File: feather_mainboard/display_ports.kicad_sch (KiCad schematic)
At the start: 1 part, among them J1 61300811121

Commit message: finished daughter board
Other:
- note added: "Need to change the connector"
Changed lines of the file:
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@@
+		)
+	)
+	(text "Need to change the connector"
+		(exclude_from_sim no)
+		(at 138.684 70.612 0)
+		(effects
+			(font
+				(size 10 10)
+				(thickness 4)
+				(bold yes)
+			)
 		)
 	)

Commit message: finished mainboard design, need to do the routing
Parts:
- removed J1: 61300811121, Custom footprints:61300811121, symbol 6130XX11121_61300811121:6130XX11121_61300811121
- added J1: 61900819521, Custom footprints:61900819521, symbol 61900819521:61900819521
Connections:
- net BUSY: now also J1.1
- net CS: now also J1.4
- net DC: now also J1.3
- net DIN: now also J1.6
- net GND: now also J1.7
- net RST: now also J1.2
- net SCLK: now also J1.5
- net VCC: now also J1.8
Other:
- note removed: "Need to change the connector"
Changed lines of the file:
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@@
-		)
-	)
-	(text "Need to change the connector"
-		(exclude_from_sim no)
-		(at 138.684 70.612 0)
-		(effects
-			(font
-				(size 10 10)
-				(thickness 4)
-				(bold yes)
-			)
 		)
 	)
@@
 	)
 	(symbol
-		(lib_id "6130XX11121_61300811121:6130XX11121_61300811121")
+		(lib_id "61900819521:61900819521")
 		(at 153.67 90.17 270)
 		(unit 1)
@@
 		(dnp no)
 		(property "Reference" "J1"
-			(at 151.13 80.264 90)
+			(at 151.384 80.01 90)
 			(effects
 				(font
@@
 			)
 		)
-		(property "Value" "61300811121"
-			(at 146.812 79.248 90)
-			(effects
-				(font
-					(size 1.27 1.27)
-				)
-				(justify left)
-				(hide yes)
-			)
-		)
-		(property "Footprint" "Custom footprints:61300811121"
+		(property "Value" "61900819521"
+			(at 153.67 90.17 0)
+			(effects
+				(font
+					(size 1.27 1.27)
+				)
+				(justify bottom)
+				(hide yes)
+			)
+		)
+		(property "Footprint" "Custom footprints:61900819521"
 			(at 153.67 90.17 0)
 			(effects
@@
 			)
 		)
-		(property "ROWS" "Single"
-			(at 153.67 90.17 0)
-			(effects
-				(font
-					(size 1.27 1.27)
-				)
-				(justify bottom)
-				(hide yes)
-			)
-		)
-		(property "GENDER" "Pin Header"
+		(property "MF" "Würth Elektronik"
+			(at 153.67 90.17 0)
+			(effects
+				(font
+					(size 1.27 1.27)
+				)
+				(justify bottom)
+				(hide yes)
+			)
+		)
+		(property "CONTACT-RESISTANCE" "20mOhm"
+			(at 153.67 90.17 0)
+			(effects
+				(font
+					(size 1.27 1.27)
+				)
+				(justify bottom)
+				(hide yes)
+			)
+		)
+		(property "Description_1" "\n                        \n                            EMI Gaskets, Sheets, Absorbers & Shielding\n                        \n"
+			(at 153.67 90.17 0)
+			(effects
+				(font
+					(size 1.27 1.27)
+				)
+				(justify bottom)
+				(hide yes)
+			)
+		)
+		(property "Package" "None"
+			(at 153.67 90.17 0)
+			(effects
+				(font
+					(size 1.27 1.27)
+				)
+				(justify bottom)
+				(hide yes)
+			)
+		)
+		(property "GENDER" "Male"
 			(at 153.67 90.17 0)
 			(effects
@@
 			)
 		)
-		(property "IR" "3A"
-			(at 153.67 90.17 0)
-			(effects
-				(font
-					(size 1.27 1.27)
-				)
-				(justify bottom)
-				(hide yes)
-			)
-		)
-		(property "VALUE" "61300811121"
+		(property "PITCH" "2.54mm"
+			(at 153.67 90.17 0)
+			(effects
+				(font
+					(size 1.27 1.27)
+				)
+				(justify bottom)
+				(hide yes)
+			)
+		)
+		(property "Check_prices" "https://www.snapeda.com/parts/61900819521/Wurth+Elektronik/view-part/?ref=eda"
+			(at 153.67 90.17 0)
+			(effects
+				(font
+					(size 1.27 1.27)
+				)
+				(justify bottom)
+				(hide yes)
+			)
+		)
+		(property "L" "20.32mm"
+			(at 153.67 90.17 0)
+			(effects
+				(font
+					(size 1.27 1.27)
+				)
+				(justify bottom)
+				(hide yes)
+			)
+		)
+		(property "Price" "None"
 			(at 153.67 90.17 0)
 			(effects
@@
 			)
 		)
+		(property "PART-NUMBER" "61900819521"
+			(at 153.67 90.17 0)
+			(effects
+				(font
+					(size 1.27 1.27)
+				)
+				(justify bottom)
+				(hide yes)
+			)
+		)
+		(property "SnapEDA_Link" "https://www.snapeda.com/parts/61900819521/Wurth+Elektronik/view-part/?ref=snap"
+			(at 153.67 90.17 0)
+			(effects
+				(font
+					(size 1.27 1.27)
+				)
+				(justify bottom)
+				(hide yes)
+			)
+		)
+		(property "DATASHEET-URL" "https://www.we-online.com/redexpert/spec/61900819521?ae"
+			(at 153.67 90.17 0)
+			(effects
+				(font
+					(size 1.27 1.27)
+				)
+				(justify bottom)
+				(hide yes)
+			)
+		)
+		(property "MP" "61900819521"
+			(at 153.67 90.17 0)
+			(effects
+				(font
+					(size 1.27 1.27)
+				)
+				(justify bottom)
+				(hide yes)
+			)
+		)
+		(property "WORKING-VOLTAGE" "250V(AC)"
+			(at 153.67 90.17 0)
+			(effects
+				(font
+					(size 1.27 1.27)
+				)
+				(justify bottom)
+				(hide yes)
+			)
+		)
 		(property "PINS" "8"
 			(at 153.67 90.17 0)
@@
 			)
 		)
-		(property "DATASHEET-URL" "https://www.we-online.com/redexpert/spec/61300811121?ae"
-			(at 153.67 90.17 0)
-			(effects
-				(font
-					(size 1.27 1.27)
-				)
-				(justify bottom)
-				(hide yes)
-			)
-		)
-		(property "PITCH" "2.54mm"
-			(at 153.67 90.17 0)
-			(effects
-				(font
-					(size 1.27 1.27)
-				)
-				(justify bottom)
-				(hide yes)
-			)
-		)
-		(property "PART-NUMBER" "61300811121"
-			(at 153.67 90.17 0)
-			(effects
-				(font
-					(size 1.27 1.27)
-				)
-				(justify bottom)
-				(hide yes)
-			)
-		)
-		(property "TYPE" "Straight"
-			(at 153.67 90.17 0)
-			(effects
-				(font
-					(size 1.27 1.27)
-				)
-				(justify bottom)
-				(hide yes)
-			)
+		(property "TYPE" "Right Angled Top Locking"
+			(at 153.67 90.17 0)
+			(effects
+				(font
+					(size 1.27 1.27)
+				)
+				(justify bottom)
+				(hide yes)
+			)
+		)
+		(property "PCB-CABLE-PANEL" "PCB"
+			(at 153.67 90.17 0)
+			(effects
+				(font
+					(size 1.27 1.27)
+				)
+				(justify bottom)
+				(hide yes)
+			)
+		)
+		(property "Availability" "In Stock"
+			(at 153.67 90.17 0)
+			(effects
+				(font
+					(size 1.27 1.27)
+				)
+				(justify bottom)
+				(hide yes)
+			)
+		)
+		(pin "6"
+		)
+		(pin "5"
 		)
 		(pin "2"
 		)
-		(pin "5"
+		(pin "1"
+		)
+		(pin "8"
+		)
+		(pin "3"
 		)
 		(pin "7"
 		)
-		(pin "3"
-		)
-		(pin "6"
-		)
-		(pin "1"
-		)
-		(pin "8"
-		)
 		(pin "4"

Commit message: finished mainboard and daughterboard
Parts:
- removed J1: 61900819521, Custom footprints:61900819521, symbol 61900819521:61900819521
- added J1: 62501021721, Custom footprints:62501021721, symbol 6250XX21721_62501021721:6250XX21721_62501021721
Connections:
- net BUSY: now also J1.2
- net CS: now also J1.5
- net DC: now also J1.4
- net DIN: now also J1.7
- net GND: now also J1.8
- net RST: now also J1.3
- net SCLK: now also J1.6
- net VCC: now also J1.9
- no-connect marks 0 -> 2

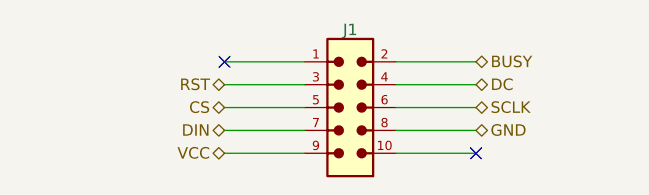
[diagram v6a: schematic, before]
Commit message: Updated the mainboard: removed unnecessary pull-ups on SD card lines; connected IIC pull-ups to enable circuit; cleaned up schematic
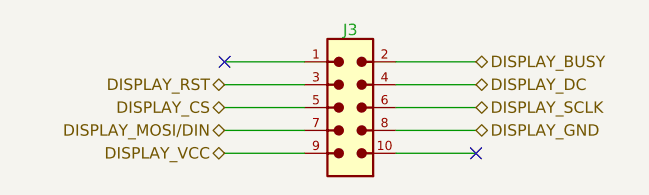
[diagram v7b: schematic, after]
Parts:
- J3: renamed from J1; footprint Custom footprints:62501021721 -> Custom footprints:62501021721_full
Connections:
- net BUSY renamed DISPLAY_BUSY
- net CS renamed DISPLAY_CS
- net DC renamed DISPLAY_DC
- net DIN renamed DISPLAY_MOSI/DIN
- net GND renamed DISPLAY_GND
- net RST renamed DISPLAY_RST
- net SCLK renamed DISPLAY_SCLK
- net VCC renamed DISPLAY_VCC
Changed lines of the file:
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@@
 		)
 	)
-	(hierarchical_label "RST"
+	(hierarchical_label "DISPLAY_RST"
 		(shape bidirectional)
 		(at 134.62 100.33 180)
+		(fields_autoplaced yes)
 		(effects
 			(font
@@
 		)
 	)
-	(hierarchical_label "DIN"
+	(hierarchical_label "DISPLAY_MOSI{slash}DIN"
 		(shape bidirectional)
 		(at 134.62 105.41 180)
+		(fields_autoplaced yes)
 		(effects
 			(font
@@
 		)
 	)
-	(hierarchical_label "GND"
+	(hierarchical_label "DISPLAY_GND"
 		(shape bidirectional)
 		(at 162.56 105.41 0)
+		(fields_autoplaced yes)
 		(effects
 			(font
@@
 		)
 	)
-	(hierarchical_label "DC"
+	(hierarchical_label "DISPLAY_DC"
 		(shape bidirectional)
 		(at 162.56 100.33 0)
+		(fields_autoplaced yes)
 		(effects
 			(font
@@
 		)
 	)
-	(hierarchical_label "CS"
+	(hierarchical_label "DISPLAY_CS"
 		(shape bidirectional)
 		(at 134.62 102.87 180)
+		(fields_autoplaced yes)
 		(effects
 			(font
@@
 		)
 	)
-	(hierarchical_label "VCC"
+	(hierarchical_label "DISPLAY_VCC"
 		(shape bidirectional)
 		(at 134.62 107.95 180)
+		(fields_autoplaced yes)
 		(effects
 			(font
@@
 		)
 	)
-	(hierarchical_label "SCLK"
+	(hierarchical_label "DISPLAY_SCLK"
 		(shape bidirectional)
 		(at 162.56 102.87 0)
+		(fields_autoplaced yes)
 		(effects
 			(font
@@
 		)
 	)
-	(hierarchical_label "BUSY"
+	(hierarchical_label "DISPLAY_BUSY"
 		(shape bidirectional)
 		(at 162.56 97.79 0)
+		(fields_autoplaced yes)
 		(effects
 			(font
@@
 		(on_board yes)
 		(dnp no)
-		(property "Reference" "J1"
+		(property "Reference" "J3"
 			(at 148.59 94.234 90)
 			(effects
@@
 			)
 		)
-		(property "Footprint" "Custom footprints:62501021721"
+		(property "Footprint" "Custom footprints:62501021721_full"
 			(at 148.59 102.87 0)
 			(effects
@@
 		(instances
 			(project "feather_mainboard"
-				(path "/e1e12730-ab4f-45db-8b66-c1e0f78e2f00/a867e0b4-aaaa-4d5d-aab5-187e8be84092"
-					(reference "J1")
+				(path "/e1e12730-ab4f-45db-8b66-c1e0f78e2f00/dc5b488a-e7a5-46d7-8d2b-6eefa2c6624d"
+					(reference "J3")
 					(unit 1)
 				)
